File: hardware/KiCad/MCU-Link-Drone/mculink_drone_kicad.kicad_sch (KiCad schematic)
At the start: 7 parts

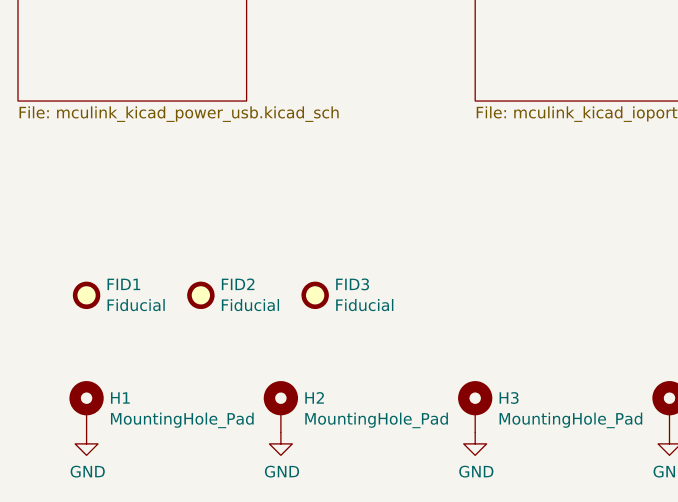
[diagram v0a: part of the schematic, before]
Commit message: fixed warnings
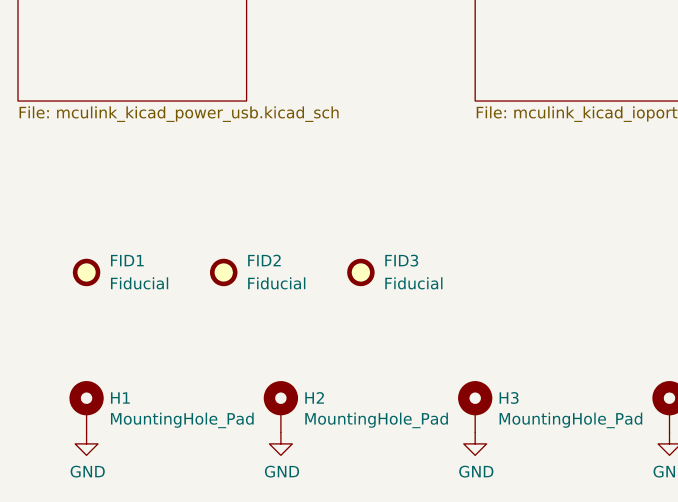
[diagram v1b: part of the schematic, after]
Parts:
- FID1, FID2, FID3: now in the parts list
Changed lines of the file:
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@@
-	)
-	(symbol
-		(lib_id "Mechanical:Fiducial")
-		(at 33.02 85.09 0)
-		(unit 1)
-		(exclude_from_sim no)
-		(in_bom no)
-		(on_board yes)
-		(dnp no)
-		(property "Reference" "FID1"
-			(at 35.179 83.9216 0)
-			(effects
-				(font
-					(size 1.27 1.27)
-				)
-				(justify left)
-			)
-		)
-		(property "Value" "Fiducial"
-			(at 35.179 86.233 0)
-			(effects
-				(font
-					(size 1.27 1.27)
-				)
-				(justify left)
-			)
-		)
-		(property "Footprint" "McuOnEclipse:Fiducial_1mm_Dia_2.54mm_Outer_CopperTop"
-			(at 33.02 85.09 0)
-			(effects
-				(font
-					(size 1.27 1.27)
-				)
-				(hide yes)
-			)
-		)
-		(property "Datasheet" ""
-			(at 33.02 85.09 0)
-			(effects
-				(font
-					(size 1.27 1.27)
-				)
-				(hide yes)
-			)
-		)
-		(property "Description" "Fiducial Marker"
-			(at 33.02 85.09 0)
-			(effects
-				(font
-					(size 1.27 1.27)
-				)
-				(hide yes)
-			)
-		)
-		(instances
-			(project "mculink_kicad"
-				(path "/5d025764-753a-4b80-8d3d-c9a8a22c9527"
-					(reference "FID1")
-					(unit 1)
-				)
-			)
-		)
 	)
 	(symbol
@@
 		)
 		(instances
-			(project "mculink_kicad"
+			(project "mculink_drone_kicad"
 				(path "/5d025764-753a-4b80-8d3d-c9a8a22c9527"
 					(reference "H1")
-					(unit 1)
-				)
-			)
-		)
-	)
-	(symbol
-		(lib_id "Mechanical:Fiducial")
-		(at 45.72 85.09 0)
-		(unit 1)
-		(exclude_from_sim no)
-		(in_bom no)
-		(on_board yes)
-		(dnp no)
-		(property "Reference" "FID2"
-			(at 47.879 83.9216 0)
-			(effects
-				(font
-					(size 1.27 1.27)
-				)
-				(justify left)
-			)
-		)
-		(property "Value" "Fiducial"
-			(at 47.879 86.233 0)
-			(effects
-				(font
-					(size 1.27 1.27)
-				)
-				(justify left)
-			)
-		)
-		(property "Footprint" "McuOnEclipse:Fiducial_1mm_Dia_2.54mm_Outer_CopperTop"
-			(at 45.72 85.09 0)
-			(effects
-				(font
-					(size 1.27 1.27)
-				)
-				(hide yes)
-			)
-		)
-		(property "Datasheet" ""
-			(at 45.72 85.09 0)
-			(effects
-				(font
-					(size 1.27 1.27)
-				)
-				(hide yes)
-			)
-		)
-		(property "Description" "Fiducial Marker"
-			(at 45.72 85.09 0)
-			(effects
-				(font
-					(size 1.27 1.27)
-				)
-				(hide yes)
-			)
-		)
-		(instances
-			(project "mculink_kicad"
-				(path "/5d025764-753a-4b80-8d3d-c9a8a22c9527"
-					(reference "FID2")
-					(unit 1)
-				)
-			)
-		)
-	)
-	(symbol
-		(lib_id "Mechanical:Fiducial")
-		(at 58.42 85.09 0)
-		(unit 1)
-		(exclude_from_sim no)
-		(in_bom no)
-		(on_board yes)
-		(dnp no)
-		(property "Reference" "FID3"
-			(at 60.579 83.9216 0)
-			(effects
-				(font
-					(size 1.27 1.27)
-				)
-				(justify left)
-			)
-		)
-		(property "Value" "Fiducial"
-			(at 60.579 86.233 0)
-			(effects
-				(font
-					(size 1.27 1.27)
-				)
-				(justify left)
-			)
-		)
-		(property "Footprint" "McuOnEclipse:Fiducial_1mm_Dia_2.54mm_Outer_CopperTop"
-			(at 58.42 85.09 0)
-			(effects
-				(font
-					(size 1.27 1.27)
-				)
-				(hide yes)
-			)
-		)
-		(property "Datasheet" ""
-			(at 58.42 85.09 0)
-			(effects
-				(font
-					(size 1.27 1.27)
-				)
-				(hide yes)
-			)
-		)
-		(property "Description" "Fiducial Marker"
-			(at 58.42 85.09 0)
-			(effects
-				(font
-					(size 1.27 1.27)
-				)
-				(hide yes)
-			)
-		)
-		(instances
-			(project "mculink_kicad"
-				(path "/5d025764-753a-4b80-8d3d-c9a8a22c9527"
-					(reference "FID3")
 					(unit 1)
 				)
@@
 		)
 		(instances
-			(project "mculink_kicad"
+			(project "mculink_drone_kicad"
 				(path "/5d025764-753a-4b80-8d3d-c9a8a22c9527"
 					(reference "H2")
@@
 		)
 		(instances
-			(project "mculink_kicad"
+			(project "mculink_drone_kicad"
 				(path "/5d025764-753a-4b80-8d3d-c9a8a22c9527"
 					(reference "H3")
@@
 		)
 		(instances
-			(project "mculink_kicad"
+			(project "mculink_drone_kicad"
 				(path "/5d025764-753a-4b80-8d3d-c9a8a22c9527"
 					(reference "H4")
@@
 		)
 		(instances
-			(project "mculink_kicad"
+			(project "mculink_drone_kicad"
 				(path "/5d025764-753a-4b80-8d3d-c9a8a22c9527"
 					(reference "#PWR0104")
@@
 		)
 		(instances
-			(project "mculink_kicad"
+			(project "mculink_drone_kicad"
 				(path "/5d025764-753a-4b80-8d3d-c9a8a22c9527"
 					(reference "#PWR0105")
@@
 		)
 		(instances
-			(project "mculink_kicad"
+			(project "mculink_drone_kicad"
 				(path "/5d025764-753a-4b80-8d3d-c9a8a22c9527"
 					(reference "#PWR0106")
@@
 		)
 		(instances
-			(project "mculink_kicad"
+			(project "mculink_drone_kicad"
 				(path "/5d025764-753a-4b80-8d3d-c9a8a22c9527"
 					(reference "#PWR0107")
+					(unit 1)
+				)
+			)
+		)
+	)
+	(symbol
+		(lib_id "Mechanical:Fiducial")
+		(at 33.02 82.55 0)
+		(unit 1)
+		(exclude_from_sim no)
+		(in_bom yes)
+		(on_board yes)
+		(dnp no)
+		(fields_autoplaced yes)
+		(property "Reference" "FID1"
+			(at 35.56 81.2799 0)
+			(effects
+				(font
+					(size 1.27 1.27)
+				)
+				(justify left)
+			)
+		)
+		(property "Value" "Fiducial"
+			(at 35.56 83.8199 0)
+			(effects
+				(font
+					(size 1.27 1.27)
+				)
+				(justify left)
+			)
+		)
+		(property "Footprint" "McuOnEclipse:Fiducial_1mm_Dia_2.54mm_Outer_CopperTop"
+			(at 33.02 82.55 0)
+			(effects
+				(font
+					(size 1.27 1.27)
+				)
+				(hide yes)
+			)
+		)
+		(property "Datasheet" "~"
+			(at 33.02 82.55 0)
+			(effects
+				(font
+					(size 1.27 1.27)
+				)
+				(hide yes)
+			)
+		)
+		(property "Description" "Fiducial Marker"
+			(at 33.02 82.55 0)
+			(effects
+				(font
+					(size 1.27 1.27)
+				)
+				(hide yes)
+			)
+		)
+		(instances
+			(project "mculink_drone_kicad"
+				(path "/5d025764-753a-4b80-8d3d-c9a8a22c9527"
+					(reference "FID1")
+					(unit 1)
+				)
+			)
+		)
+	)
+	(symbol
+		(lib_id "Mechanical:Fiducial")
+		(at 48.26 82.55 0)
+		(unit 1)
+		(exclude_from_sim no)
+		(in_bom yes)
+		(on_board yes)
+		(dnp no)
+		(fields_autoplaced yes)
+		(property "Reference" "FID2"
+			(at 50.8 81.2799 0)
+			(effects
+				(font
+					(size 1.27 1.27)
+				)
+				(justify left)
+			)
+		)
+		(property "Value" "Fiducial"
+			(at 50.8 83.8199 0)
+			(effects
+				(font
+					(size 1.27 1.27)
+				)
+				(justify left)
+			)
+		)
+		(property "Footprint" "McuOnEclipse:Fiducial_1mm_Dia_2.54mm_Outer_CopperTop"
+			(at 48.26 82.55 0)
+			(effects
+				(font
+					(size 1.27 1.27)
+				)
+				(hide yes)
+			)
+		)
+		(property "Datasheet" "~"
+			(at 48.26 82.55 0)
+			(effects
+				(font
+					(size 1.27 1.27)
+				)
+				(hide yes)
+			)
+		)
+		(property "Description" "Fiducial Marker"
+			(at 48.26 82.55 0)
+			(effects
+				(font
+					(size 1.27 1.27)
+				)
+				(hide yes)
+			)
+		)
+		(instances
+			(project "mculink_drone_kicad"
+				(path "/5d025764-753a-4b80-8d3d-c9a8a22c9527"
+					(reference "FID2")
+					(unit 1)
+				)
+			)
+		)
+	)
+	(symbol
+		(lib_id "Mechanical:Fiducial")
+		(at 63.5 82.55 0)
+		(unit 1)
+		(exclude_from_sim no)
+		(in_bom yes)
+		(on_board yes)
+		(dnp no)
+		(fields_autoplaced yes)
+		(property "Reference" "FID3"
+			(at 66.04 81.2799 0)
+			(effects
+				(font
+					(size 1.27 1.27)
+				)
+				(justify left)
+			)
+		)
+		(property "Value" "Fiducial"
+			(at 66.04 83.8199 0)
+			(effects
+				(font
+					(size 1.27 1.27)
+				)
+				(justify left)
+			)
+		)
+		(property "Footprint" "McuOnEclipse:Fiducial_1mm_Dia_2.54mm_Outer_CopperTop"
+			(at 63.5 82.55 0)
+			(effects
+				(font
+					(size 1.27 1.27)
+				)
+				(hide yes)
+			)
+		)
+		(property "Datasheet" "~"
+			(at 63.5 82.55 0)
+			(effects
+				(font
+					(size 1.27 1.27)
+				)
+				(hide yes)
+			)
+		)
+		(property "Description" "Fiducial Marker"
+			(at 63.5 82.55 0)
+			(effects
+				(font
+					(size 1.27 1.27)
+				)
+				(hide yes)
+			)
+		)
+		(instances
+			(project "mculink_drone_kicad"
+				(path "/5d025764-753a-4b80-8d3d-c9a8a22c9527"
+					(reference "FID3")
 					(unit 1)
 				)
@@
 		)
 		(instances
-			(project "mculink_kicad"
+			(project "mculink_drone_kicad"
 				(path "/5d025764-753a-4b80-8d3d-c9a8a22c9527"
 					(page "2")
@@
 		)
 		(instances
-			(project "mculink_kicad"
+			(project "mculink_drone_kicad"
 				(path "/5d025764-753a-4b80-8d3d-c9a8a22c9527"
 					(page "3")
@@
 		)
 		(instances
-			(project "mculink_kicad"
+			(project "mculink_drone_kicad"
 				(path "/5d025764-753a-4b80-8d3d-c9a8a22c9527"
 					(page "4")
@@
 		)
 		(instances
-			(project "mculink_kicad"
+			(project "mculink_drone_kicad"
 				(path "/5d025764-753a-4b80-8d3d-c9a8a22c9527"
 					(page "5")

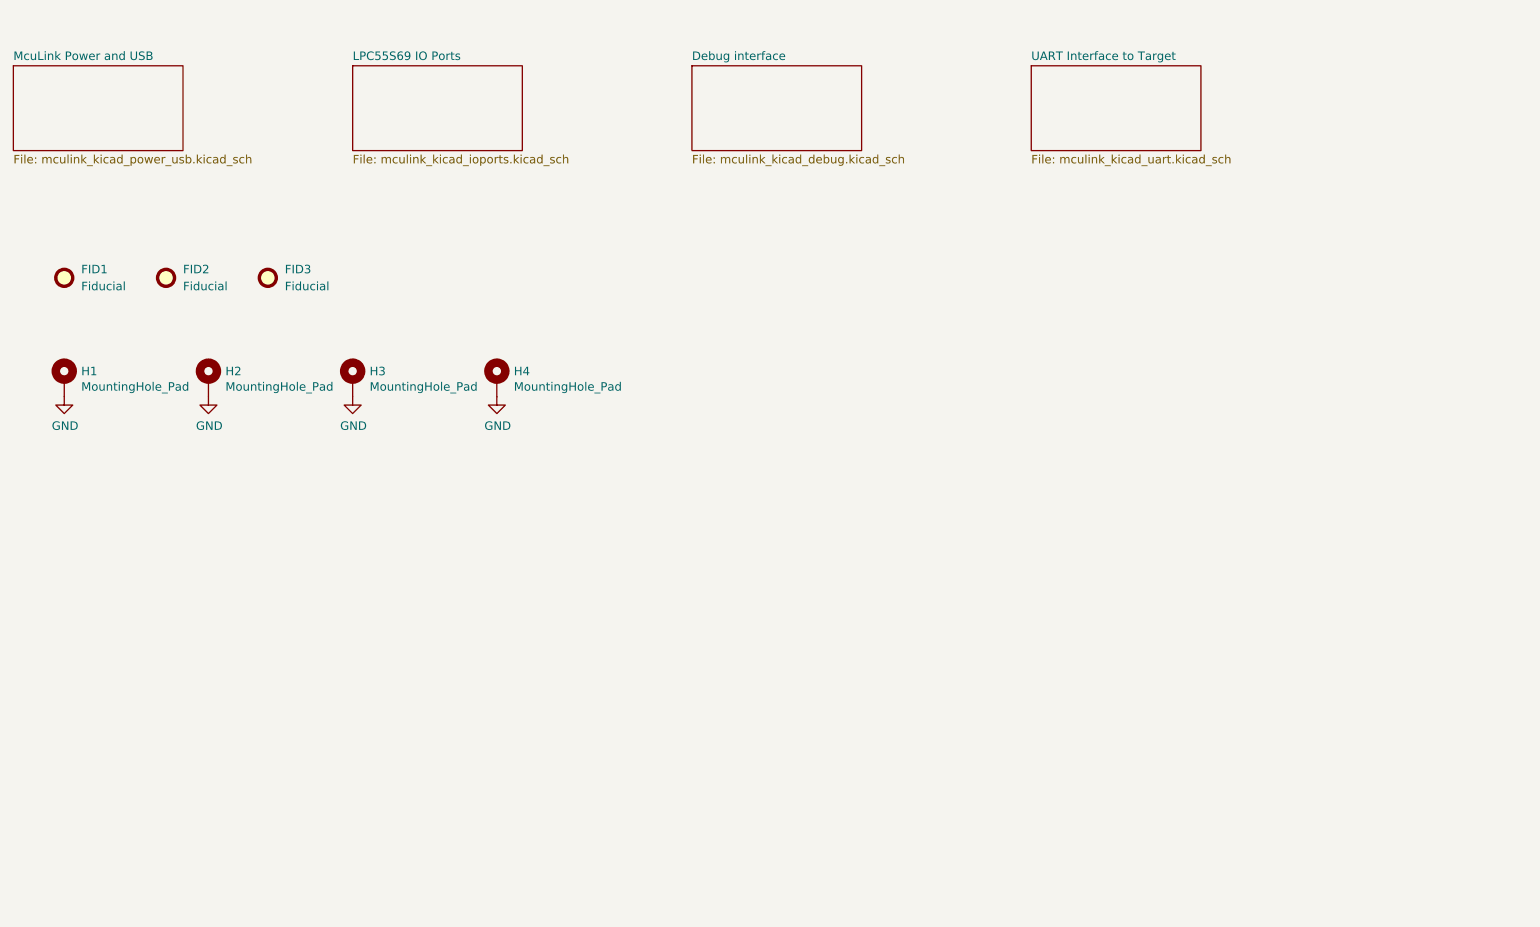
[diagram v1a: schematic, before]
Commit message: added 3D models
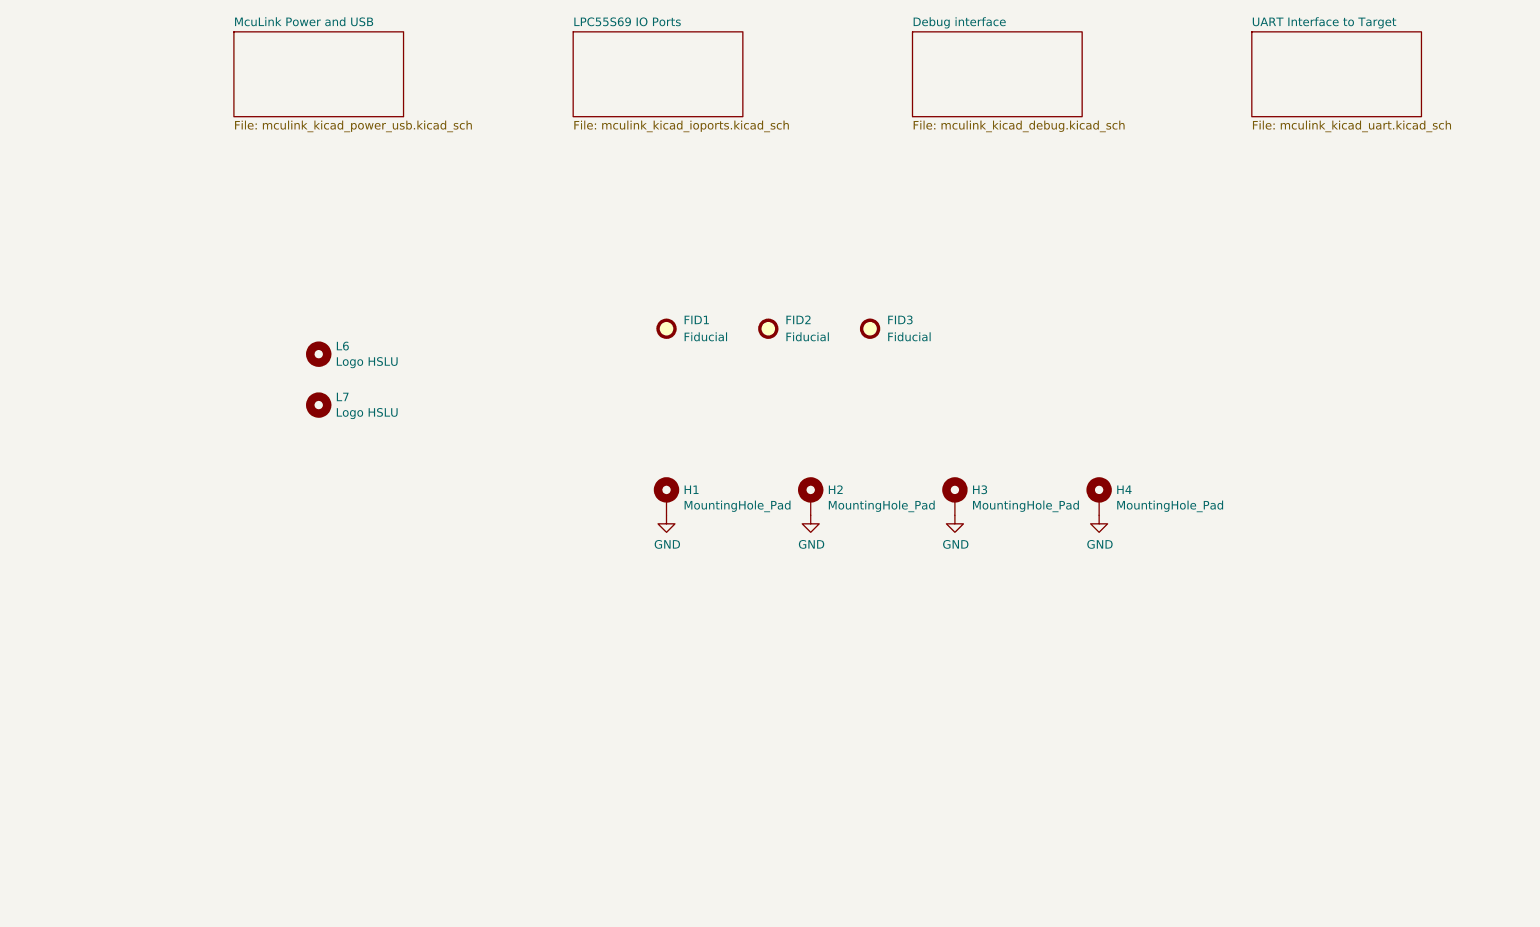
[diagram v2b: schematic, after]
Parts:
- added L6: Logo HSLU, McuOnEclipse:Hochschule_Luzern_New, symbol Mechanical:MountingHole
- added L7: Logo HSLU, McuOnEclipse:Hochschule_Luzern_Small, symbol Mechanical:MountingHole
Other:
- moved on the sheet: FID1, FID2, FID3, H1, H2, H3, H4

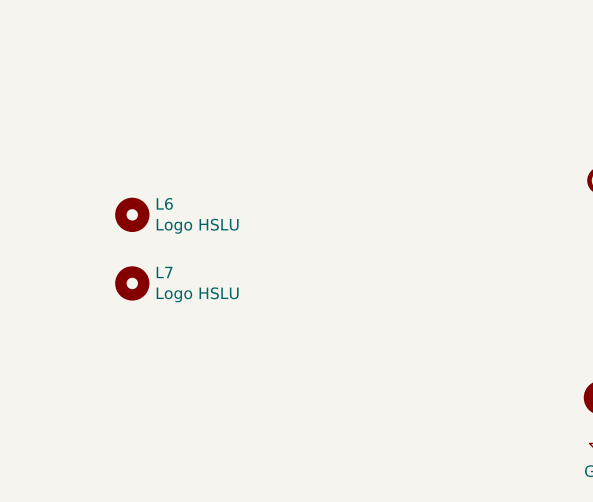
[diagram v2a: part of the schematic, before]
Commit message: fixed warnings
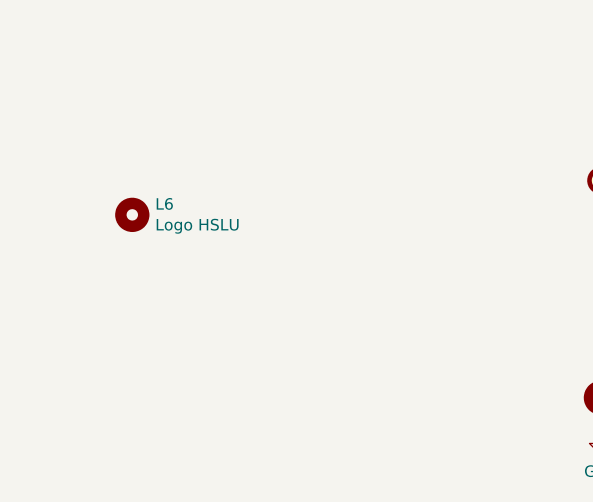
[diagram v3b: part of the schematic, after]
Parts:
- removed L7: Logo HSLU, McuOnEclipse:Hochschule_Luzern_Small, symbol Mechanical:MountingHole
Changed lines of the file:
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@@
-		)
-	)
-	(symbol
-		(lib_id "Mechanical:MountingHole")
-		(at 71.12 101.6 0)
-		(unit 1)
-		(exclude_from_sim no)
-		(in_bom no)
-		(on_board yes)
-		(dnp no)
-		(property "Reference" "L7"
-			(at 73.66 100.4316 0)
-			(effects
-				(font
-					(size 1.27 1.27)
-				)
-				(justify left)
-			)
-		)
-		(property "Value" "Logo HSLU"
-			(at 73.66 102.743 0)
-			(effects
-				(font
-					(size 1.27 1.27)
-				)
-				(justify left)
-			)
-		)
-		(property "Footprint" "McuOnEclipse:Hochschule_Luzern_Small"
-			(at 71.12 101.6 0)
-			(effects
-				(font
-					(size 1.27 1.27)
-				)
-				(hide yes)
-			)
-		)
-		(property "Datasheet" "~"
-			(at 71.12 101.6 0)
-			(effects
-				(font
-					(size 1.27 1.27)
-				)
-				(hide yes)
-			)
-		)
-		(property "Description" ""
-			(at 71.12 101.6 0)
-			(effects
-				(font
-					(size 1.27 1.27)
-				)
-				(hide yes)
-			)
-		)
-		(instances
-			(project "mculink_drone_kicad"
-				(path "/5d025764-753a-4b80-8d3d-c9a8a22c9527"
-					(reference "L7")
-					(unit 1)
-				)
-			)
 		)
 	)

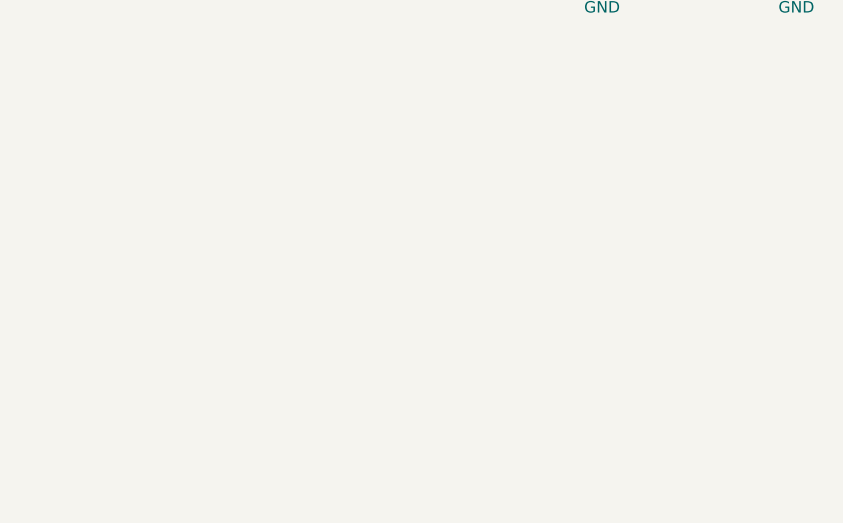
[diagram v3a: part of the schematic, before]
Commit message: updated schematics
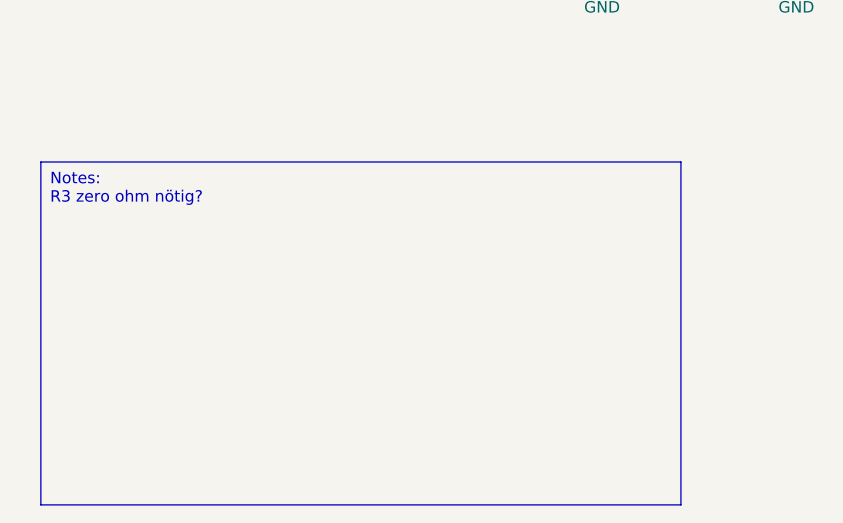
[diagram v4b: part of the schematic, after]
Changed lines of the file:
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@@
+		)
+	)
+	(text_box "Notes:\nR3 zero ohm nötig?\n"
+		(exclude_from_sim no)
+		(at 60.96 139.7 0)
+		(size 71.12 38.1)
+		(stroke
+			(width 0)
+			(type default)
+		)
+		(fill
+			(type none)
+		)
+		(effects
+			(font
+				(size 1.27 1.27)
+			)
+			(justify left top)
 		)
 	)
